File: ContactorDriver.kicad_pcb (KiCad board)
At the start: 2 copper layers, 66 x 100 mm, 40 parts, among them J1 PowerConn, J2 DashboardConn, J3 DashboardConn, J4 ContactorConn, J5 PrechargeConn, J6 PrechargeResistorConn, J7 PrechargeResistor, J8 PrechargeResistor, Q1 NTR4003NT1G, Q2 NTR4003NT1G, Q3 CSD18511KTT, Q4 CSD18511KTT

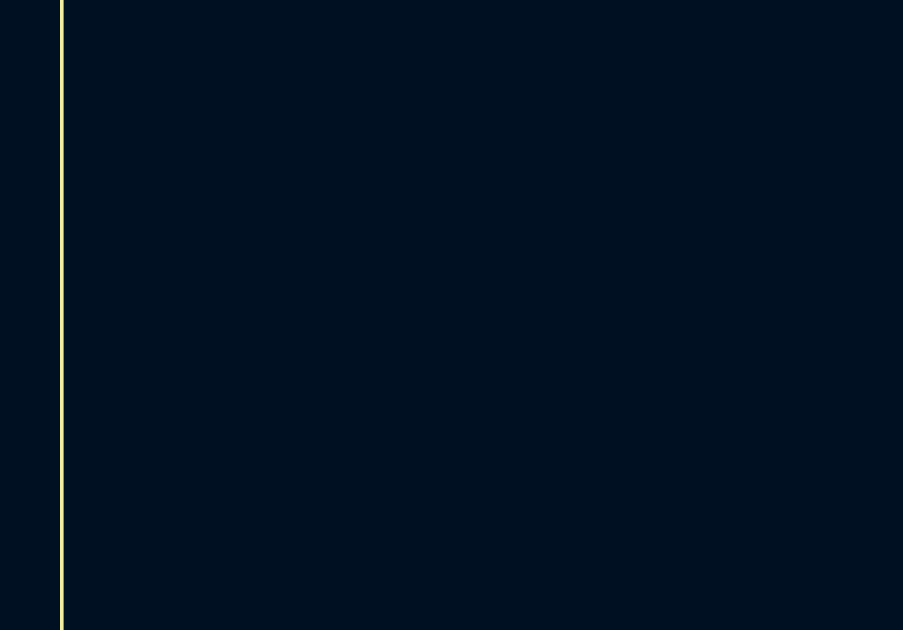
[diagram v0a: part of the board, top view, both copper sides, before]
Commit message: Formats version history better, adds datasheets for all components on schematic, and puts board dimension on user comments layer
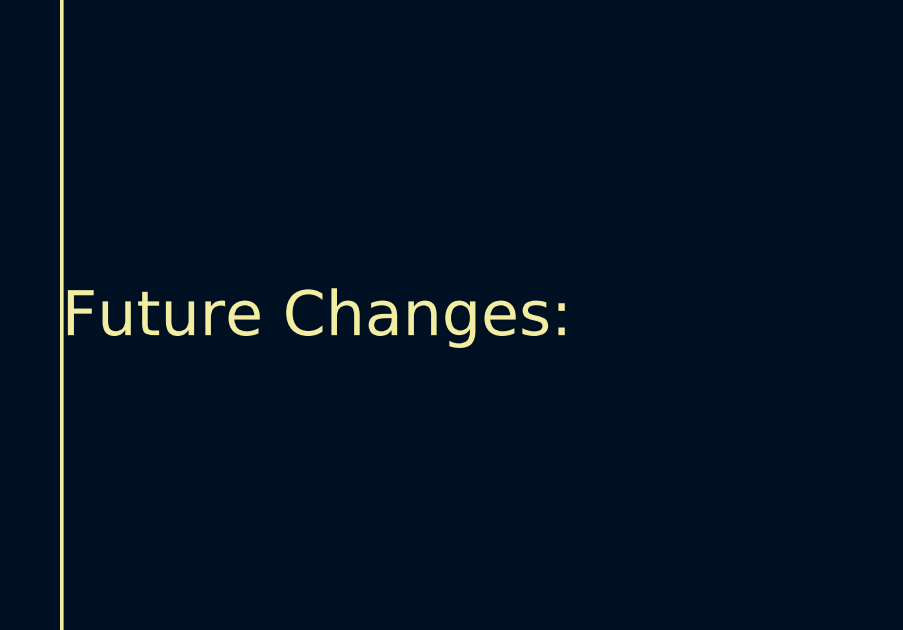
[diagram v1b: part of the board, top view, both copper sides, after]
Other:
- board text added: "Future Changes:"
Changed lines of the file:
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@@
     (effects (font (size 1 1) (thickness 0.15)))
+  )
+  (gr_text "Future Changes:\n" (at 12.7 45.72) (layer "F.SilkS")
+    (effects (font (size 1.5 1.5) (thickness 0.15)) (justify left bottom))
   )
   (gr_text "EN" (at 218 99) (layer "F.SilkS")
@@
     (effects (font (size 1 1) (thickness 0.15)))
   )
-  (dimension (type aligned) (layer "F.SilkS")
+  (dimension (type aligned) (layer "Cmts.User")
     (pts (xy 164 68) (xy 230 68))
     (height -12.12)
-    (gr_text "66.0000 mm" (at 197 54.73) (layer "F.SilkS")
+    (gr_text "66.0000 mm" (at 197 54.73) (layer "Cmts.User")
       (effects (font (size 1 1) (thickness 0.15)))
     )
@@
     (style (thickness 0.12) (arrow_length 1.27) (text_position_mode 0) (extension_height 0.58642) (extension_offset 0.5) keep_text_aligned)
   )
-  (dimension (type aligned) (layer "F.SilkS")
+  (dimension (type aligned) (layer "Cmts.User")
     (pts (xy 230 68) (xy 230 168))
     (height -11.3)
-    (gr_text "100.0000 mm" (at 240.15 118 90) (layer "F.SilkS")
+    (gr_text "100.0000 mm" (at 240.15 118 90) (layer "Cmts.User")
       (effects (font (size 1 1) (thickness 0.15)))
     )

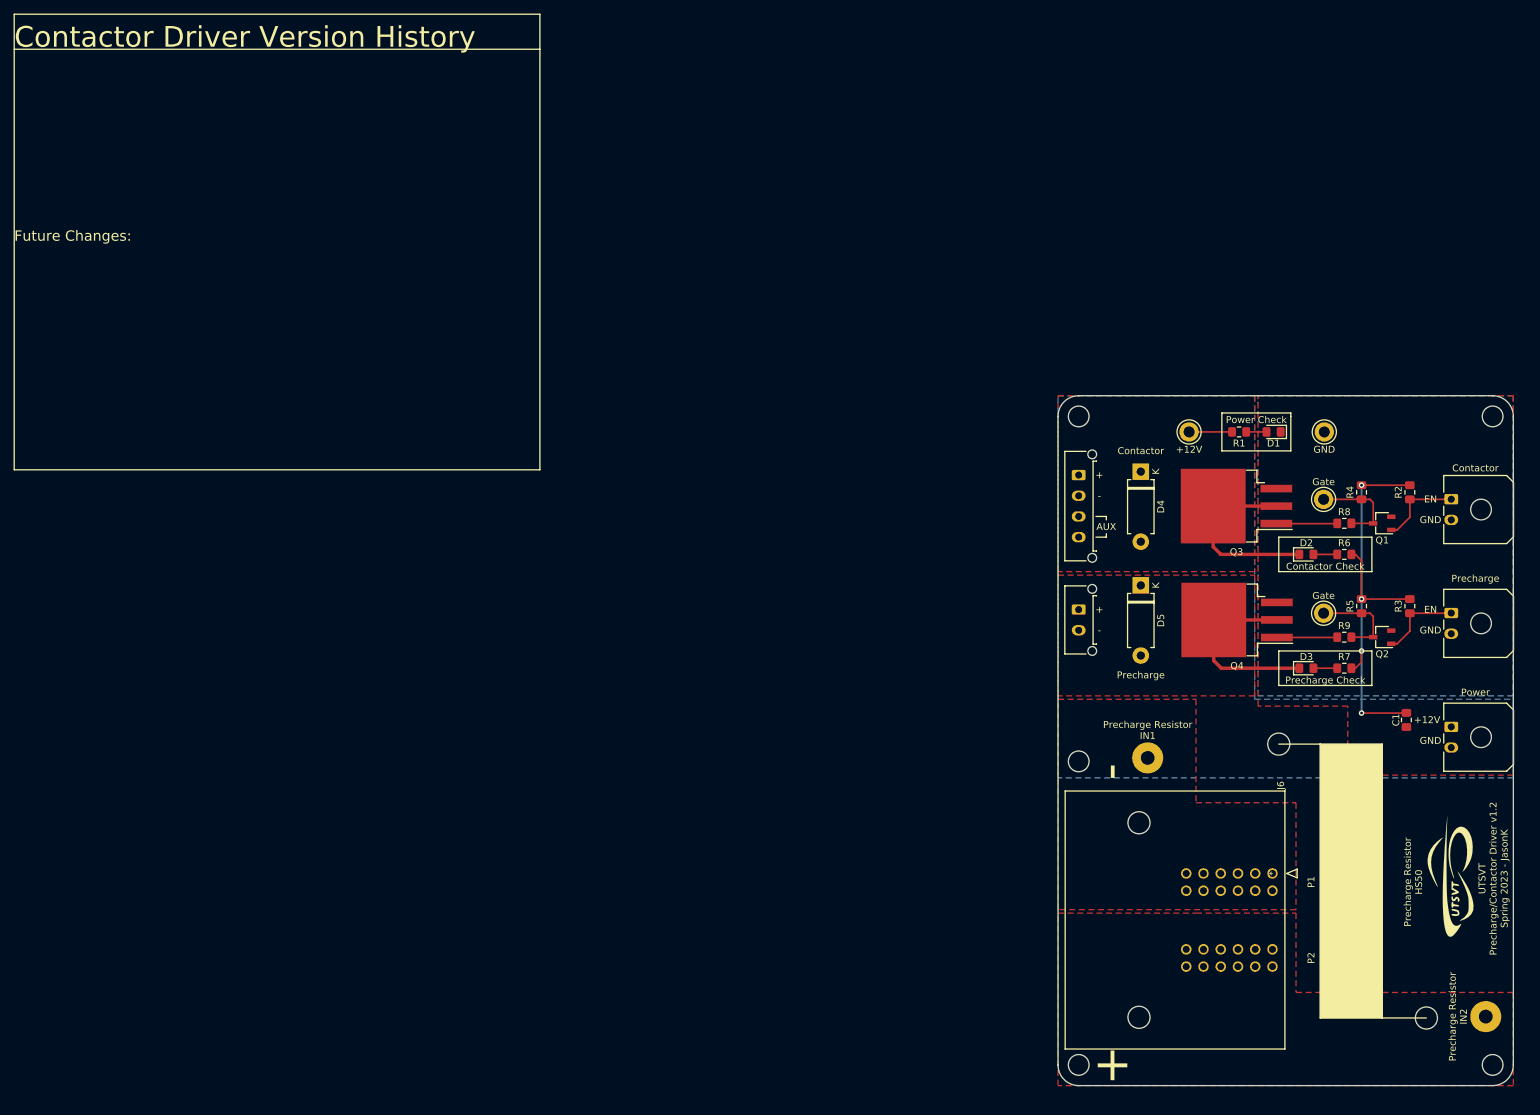
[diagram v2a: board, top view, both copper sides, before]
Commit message: Updated Contactor Driver Schematic & Layout (#3)
* Updated Contactor Driver Schematic

* Added ferrite beads

* Changed input control logic

* Changed input logic to normally open

* Removed PU resistor

* Moved comments

* Used INA instead of 2 comparators

* Updated layout

* Did layout

* Created layout

* Fixed comments

* Updated UTSVT KiCAD Libararies

---------

Co-authored-by: Manthan Upadhyaya <manth@DESKTOP-RR47J6M>
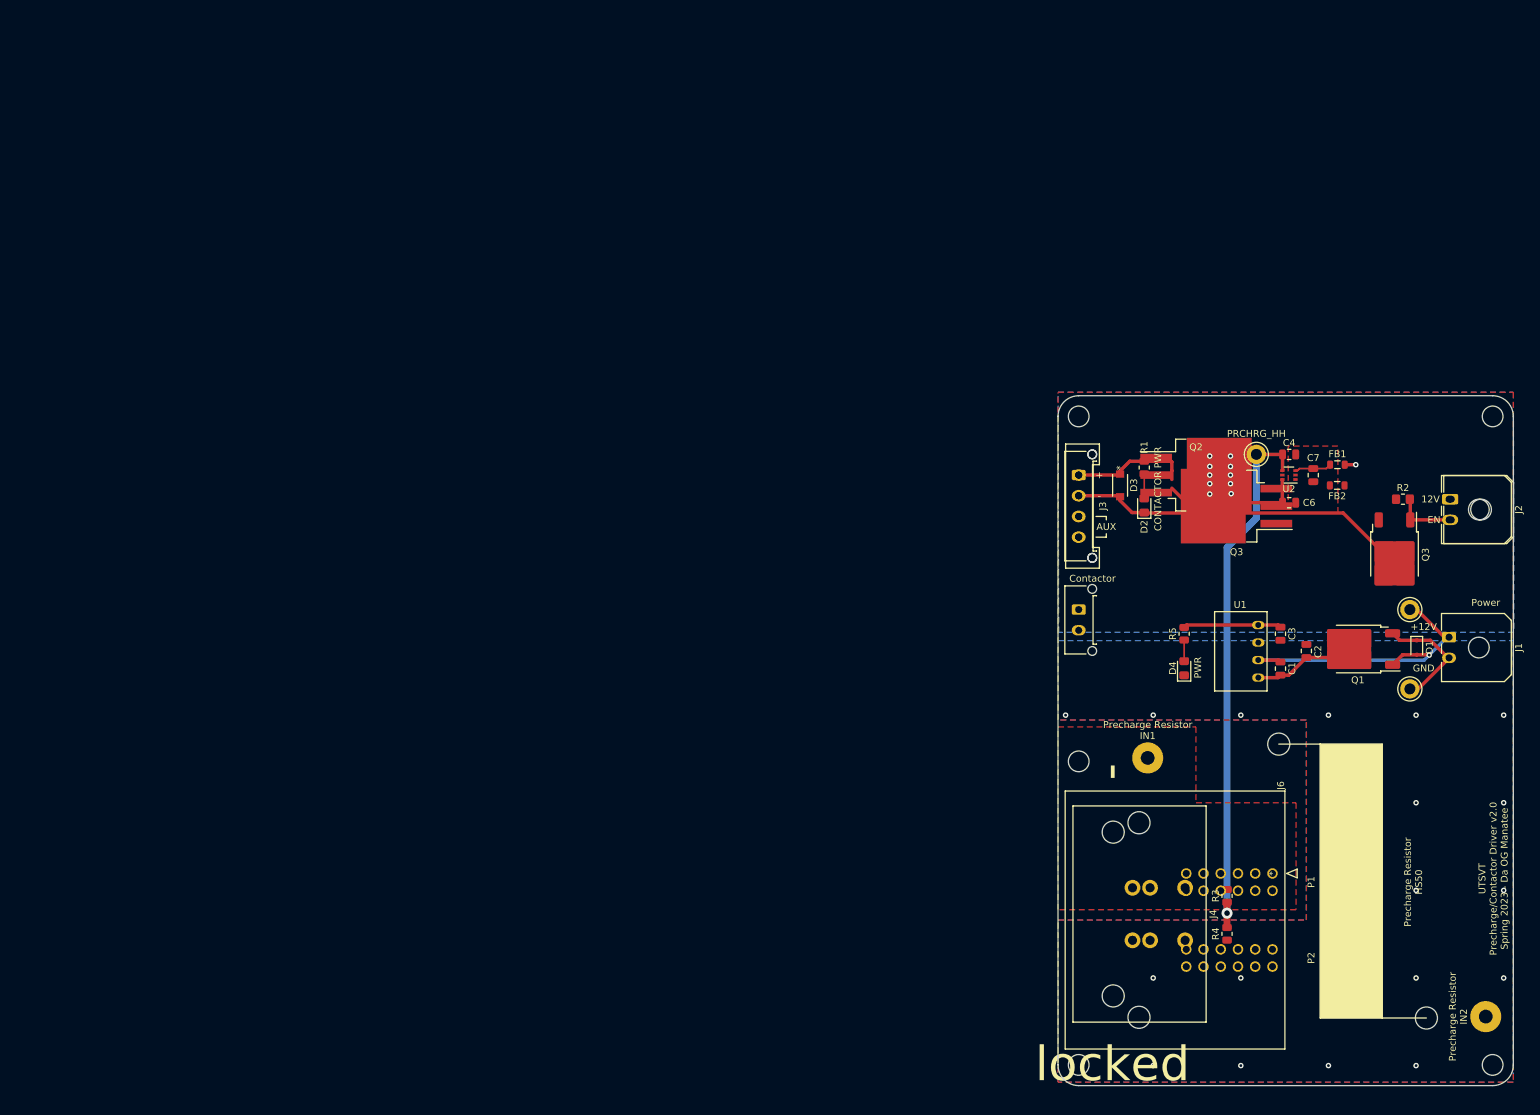
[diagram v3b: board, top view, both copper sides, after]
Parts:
- removed the D2 at (200.0, 91.0)
- removed D5: R5000F, Diode_THT:D_DO-15_P10.16mm_Horizontal
- removed G***: LOGO, UTSVT_Special:UTSVT_Logo_Symbol
- removed G***: LOGO, UTSVT_Special:Hallock_Image
- removed Q4: CSD18511KTT, Package_TO_SOT_SMD:TO-263-3_TabPin2
- removed the R1 at (190.2, 73.2)
- removed R6: 10k, Resistor_SMD:R_0805_2012Metric_Pad1.15x1.40mm_HandSolder
- removed R8, R9: 0, Resistor_SMD:R_0805_2012Metric_Pad1.15x1.40mm_HandSolder
- removed TP3: TP_+12V, TestPoint:TestPoint_Keystone_5005-5009_Compact
- removed TP4: TP_GND, TestPoint:TestPoint_Keystone_5005-5009_Compact
- added C1: 10u, Capacitor_SMD:C_0805_2012Metric, F.Cu at (196.2, 107.5)
- added C2: 2.2n, Capacitor_SMD:C_0805_2012Metric, F.Cu at (200.0, 105.0)
- added C4: .1u, Capacitor_SMD:C_0805_2012Metric, F.Cu at (197.5, 76.5)
- added C6: 1u, Capacitor_SMD:C_0805_2012Metric, F.Cu at (197.5, 83.5)
- added C7: .1u, Capacitor_SMD:C_0805_2012Metric, F.Cu at (201.0, 79.5)
- added D3: V2F22HM3/H, UTSVT_Passive:V2F22HM, F.Cu at (173.0, 81.0)
- added FB1: FerriteBead_Small, Inductor_SMD:L_0805_2012Metric, F.Cu at (204.5, 78.0)
- added FB2: FerriteBead_Small, Inductor_SMD:L_0805_2012Metric, F.Cu at (204.5, 81.0)
- added J3: ContactorConn, UTSVT_Connectors:Molex_MicroFit3.0_1x4xP3.00mm_PolarizingPeg_Vertical, F.Cu at (167.0, 79.5)
- added J4: PrechargeResistorConn, UTSVT_Connectors:PhoenixContact_PowerCombicon5_GF_2x7.62mm, F.Cu at (182.4, 139.3)
- added PRCHRG_HH: PRCHRG_HH, TestPoint:TestPoint_Keystone_5005-5009_Compact, F.Cu at (192.8, 76.5)
- added Q3: CSD18511KTT, Package_TO_SOT_SMD:TO-252-2, F.Cu at (212.8, 91.0)
- added U1: RI3-1212S, UTSVT_ICs:RI3_DC_Converter, F.Cu at (193.0, 105.0)
- added U2: INA215, Package_TO_SOT_SMD:SOT-363_SC-70-6, F.Cu at (197.5, 79.5)
- C3: renamed from C1; value 1u -> 10u; footprint Capacitor_SMD:C_0805_2012Metric_Pad1.15x1.40mm_HandSolder -> Capacitor_SMD:C_0805_2012Metric
- D1: value Green -> SD12_SOD323; footprint LED_SMD:LED_0805_2012Metric_Pad1.15x1.40mm_HandSolder -> Diode_SMD:D_SOD-323
- D4: value R5000F -> Green; footprint Diode_THT:D_DO-15_P10.16mm_Horizontal -> LED_SMD:LED_0805_2012Metric_Pad1.15x1.40mm_HandSolder
- Q1: value NTR4003NT1G -> CSD18511KTT; footprint Package_TO_SOT_SMD:TSOT-23 -> Package_TO_SOT_SMD:TO-252-2
- Q2: value NTR4003NT1G -> PMOS
- R1: renamed from R7; footprint Resistor_SMD:R_0805_2012Metric_Pad1.15x1.40mm_HandSolder -> Resistor_SMD:R_0805_2012Metric
- R2: value 10k -> 100k; footprint Resistor_SMD:R_0805_2012Metric_Pad1.15x1.40mm_HandSolder -> Resistor_SMD:R_0805_2012Metric_Pad1.20x1.40mm_HandSolder
- R3: value 10k -> 100k; footprint Resistor_SMD:R_0805_2012Metric_Pad1.15x1.40mm_HandSolder -> Resistor_SMD:R_0805_2012Metric
- R4: value 10k -> 2.2k; footprint Resistor_SMD:R_0805_2012Metric_Pad1.15x1.40mm_HandSolder -> Resistor_SMD:R_0805_2012Metric
- R5: footprint Resistor_SMD:R_0805_2012Metric_Pad1.15x1.40mm_HandSolder -> Resistor_SMD:R_0805_2012Metric
- TP1: value TP_Gate -> 12V_UNISO
- TP2: value TP_Gate -> GND_UNISO
- moved R4 66.9 mm to (188.5, 146.0)
- moved R3 49.7 mm to (188.5, 140.5)
- moved R1 41.1 mm to (176.5, 78.4), turned to 90 degrees
- moved D1 37.5 mm to (216.0, 104.5), turned to -90 degrees
- moved Q2 35.8 mm to (184.0, 79.5), turned to 0 degrees
- moved D2 33.3 mm to (176.5, 83.9), turned to 90 degrees
- moved D4 29.2 mm to (182.3, 107.5), turned to 90 degrees
- moved R5 26.0 mm to (182.3, 102.5)
- moved C3 22.1 mm to (196.2, 102.5)
- moved TP1 20.3 mm to (215.0, 99.0)
- moved Q1 18.6 mm to (207.5, 104.7)
- moved TP2 16.6 mm to (215.0, 110.5)
- moved J2 16.5 mm to (220.7, 83.0)
- moved J1 13.0 mm to (220.7, 103.0)
- moved R2 1.41 mm to (214.0, 83.0), turned to 0 degrees
- renumbered D3 to D2, H2 to H1, H1 to H2, J3 to J2, J7 to J5, J8 to J6
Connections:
- D1 pad 1: GND -> Net-(D1-A1)
- D1 pad 2: Net-(D1-Pad2) -> Net-(D1-A2)
- D2 pad 1: Net-(D3-Pad1) -> /CONTACTOR_V-
- D4 pad 1: +12V -> GND
- D4 pad 2: Net-(D2-Pad1) -> Net-(D4-A)
- J1 pad 1: +12V -> Net-(D1-A2)
- J1 pad 2: GND -> Net-(D1-A1)
- J2 pad 1: Net-(J3-Pad1) -> +12V
- J2 pad 2: GND -> Net-(J2-Pin_2)
- J5 pad 1: Net-(J6-Pad1) -> Net-(J4-Pin_1)
- J6 pad 1: Net-(J6-Pad2) -> GND
- Q1 pad 1: Net-(J2-Pad1) -> Net-(D1-A2)
- Q1 pad 2: GND -> Net-(Q1-D)
- Q1 pad 3: Net-(Q1-Pad3) -> Net-(D1-A1)
- Q2 pad 1: Net-(J3-Pad1) -> Net-(Q4-Pad1)
- Q2 pad 2: GND -> Net-(D3-Pad1)
- Q2 pad 3: Net-(Q2-Pad3) -> GND
- R1 pad 2: +12V -> /CONTACTOR_V+
- R2 pad 1: Net-(J2-Pad1) -> GND
- R2 pad 2: +12V -> Net-(J2-Pin_2)
- R3 pad 1: Net-(J3-Pad1) -> /PRCHRG_HH
- R3 pad 2: +12V -> Net-(J4-Pin_1)
- R4 pad 1: Net-(Q1-Pad3) -> GND
- R4 pad 2: +12V -> /PRCHRG_HH
- R5 pad 1: Net-(Q2-Pad3) -> Net-(D4-A)
- TP1 pad 1: Net-(Q1-Pad3) -> Net-(D1-A2)
- TP2 pad 1: Net-(Q2-Pad3) -> Net-(D1-A1)
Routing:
- net /PRCHRG_HH: track 0.00 -> 78.1 mm, vias 0 -> 1
- net +12V: track 70.6 -> 16.4 mm, vias 4 -> 11
- net /CONTACTOR_V-: track 0.00 -> 52.4 mm
- net Net-(D1-A2): track 0.00 -> 45.6 mm, vias 0 -> 1
- net Net-(D2-Pad1): track 28.0 -> 0.00 mm
- net Net-(D3-Pad1): track 27.9 -> 0.00 mm
- net /EN_CURR: track 0.00 -> 20.3 mm
- net Net-(D1-A1): track 0.00 -> 17.2 mm
- net /CONTACTOR_V+: track 0.00 -> 17.2 mm
- net Net-(Q2-Pad3): track 13.6 -> 0.00 mm
- net Net-(Q1-Pad3): track 13.6 -> 0.00 mm
- net Net-(Q1-D): track 0.00 -> 12.8 mm
- net Net-(J3-Pad1): track 12.1 -> 0.00 mm
- net Net-(J2-Pad1): track 12.1 -> 0.00 mm
- net Net-(Q3-Pad1): track 8.84 -> 0.00 mm
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- added copper zone on F.Cu, net +12V
- added copper zone on F.Cu, net Net-(J4-Pin_1)
- added copper zone on F.Cu, net Net-(U2-REF)
- removed copper zone on F.Cu, net Net-(D2-Pad1)
- removed copper zone on F.Cu, net Net-(D3-Pad1)
- removed copper zone on F.Cu, net Net-(J6-Pad1)
- removed copper zone on F.Cu, net Net-(J6-Pad2)
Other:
- board text added: "12V"
- board text added: "CONTACTOR PWR"
- board text added: "PWR"
- board text added: "UTSVT Precharge/Contactor Driver v2.0 Spring 2023 - Da OG Manatee"
- board text added: "locked"
- board text removed: "Contactor Check"
- board text removed: "Contactor Driver Version History"
- board text removed: "Future Changes:"
- board text removed: "Gate"
- board text removed: "Power Check"
- board text removed: "Precharge"
- board text removed: "Precharge Check"
- board text removed: "UTSVT Precharge/Contactor Driver v1.2 Spring 2023 - JasonK"

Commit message: Fixed pcb file
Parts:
- removed the J2 at (221.0, 83.0)
- removed the J4 at (167.0, 79.5)
- removed the J5 at (167.0, 99.0)
- removed the J6 at (195.1, 137.3)
- removed the Q3 at (189.9, 84.0)
- Q2: footprint Package_TO_SOT_SMD:TSOT-23 -> Package_SO:SO-8_5.3x6.2mm_P1.27mm
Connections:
- Q2 pad 1: Net-(Q4-Pad1) -> /CONTACTOR_V+
- Q2 pad 2: Net-(D3-Pad1) -> /CONTACTOR_V+
- Q2 pad 3: GND -> /CONTACTOR_V+
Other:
- board text added: "Contactor Driver Version History"
- board text added: "Future Changes:"
